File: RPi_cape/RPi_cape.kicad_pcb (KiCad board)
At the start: 4 copper layers, 104 x 255 mm, 523 parts, among them J1 Conn_01x04, J10 Conn_01x02, J11 Conn_01x02, J12 Conn_01x02, J13 Conn_01x02, J14 Conn_01x02, J16 Conn_01x06, J17 Pressure_sensor_barb, J18 Pressure_sensor_barb, J19 Pressure_sensor_barb, J2 Conn_01x02, J20 Pressure_sensor_barb, J3 Conn_01x02, J4 Conn_01x02, J5 Conn_01x03, J6 Conn_01x03, J7 Conn_01x02, J8 Conn_02x20_Odd_Even, J9 Conn_01x02, P15 Conn_02x05_Odd_Even, Q1 MMBT3904, Q10 MMBT3904, Q11 MMBT3904, Q12 MMBT3906, Q13 MMBT3904, Q2 MMBT3904, Q5 MMBT3904, Q6 MMBT3904, Q7 DNP, Q8 MMBT3904, Q9 MMBT3904, U1 TL431A, U10 MS5803-05BA, U11 LM2903, U12 LMC7101B, U13 LMC7101B, U14 BMP388, U15 MS5803-05BA, U16 BMP388, U17 LM2903, U18 74LVC1G08, U19 TPS1H100B, U2 ADC128D818, U20 74LVC1G08, U21 TPS1H100B, U22 74LVC1G08, U23 TPS1H100B, U24 TL431A, U25 LM2903, U26 MIC1557, U27 MIC1557, U28 LM4871M, U29 LP5907MFX-3.3, U3 ADC128D818, U30 LP5907MFX-1.8, U31 DNP (5M40ZE64), U32 MIC1557, U33 5M80ZT100 / 5M240ZT100, U34 LMZ14203, U35 LMZ14203, U36 LMC7101B, U37 LMC7101B, U38 LMC7101B, U4 AD8552A, U5 LM2903, U6 LMC7101B, U7 LMC7101B, U8 74LVC1G08, U9 TPS1H100B

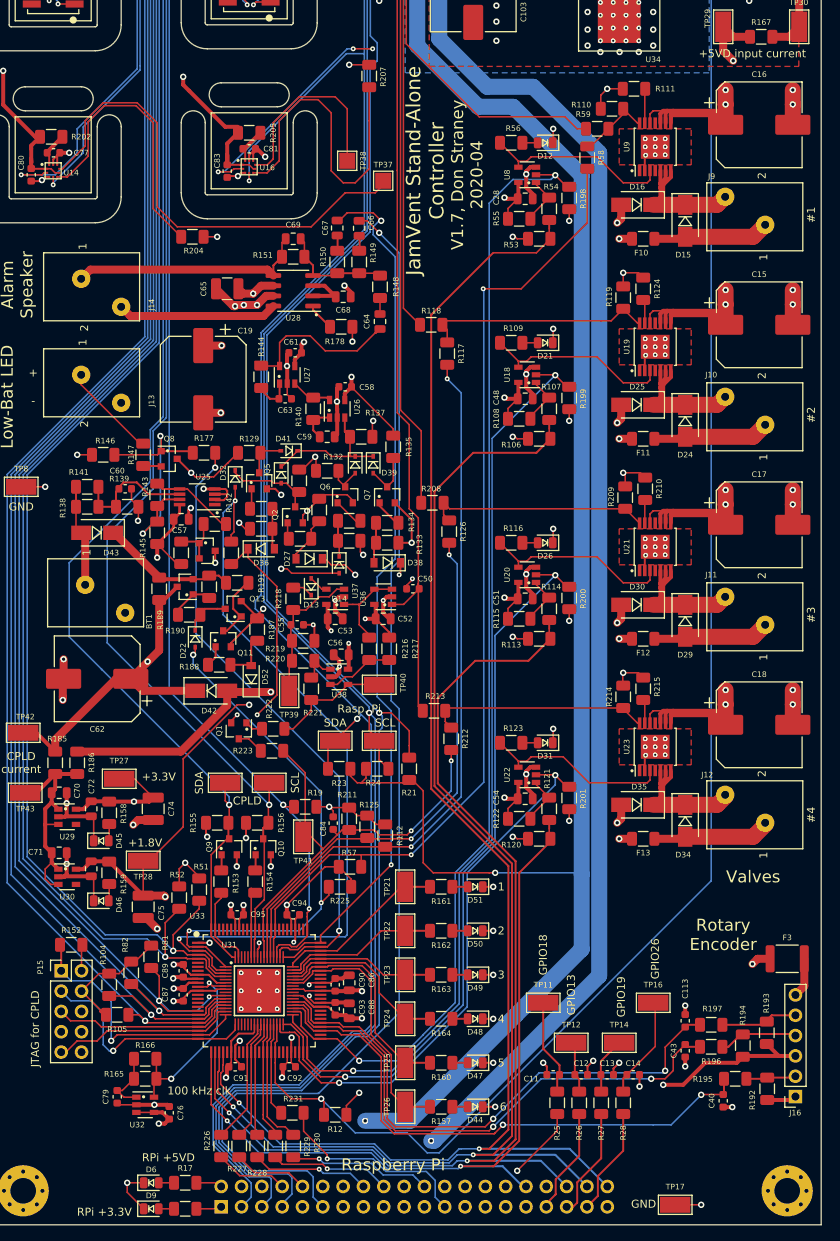
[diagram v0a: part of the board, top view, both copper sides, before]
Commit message: Analog upgrades and extra encoder connectors
Renamed a few files
Removed "costing BOM" as difficult to keep up to date, easy to regenerate
Toughened under-voltage detect circuits by adding hysteresis to +5V detect for +BATT diode-OR (R236), filtering to power-down alarm detect input (C85)
Added connector options (J15, J21) for Grayhill C14-series rotary encoder with cable
Changed R190 from 3K to 2.4K to increase overhead on base current required for saturation, and consolidate BOM
Added 3 solderable testpoints for expanding CPLD pin options (TP44-46), adjusted some CPLD pin assignments to allow physical routing to pins
Fixed valve motion detector by changing comparator's hysteresis to AC-only, changing NPN's series resistor to 1K (allows low-enough DC level to count as logic low), and adding optional filtering cap C115 to offset divider
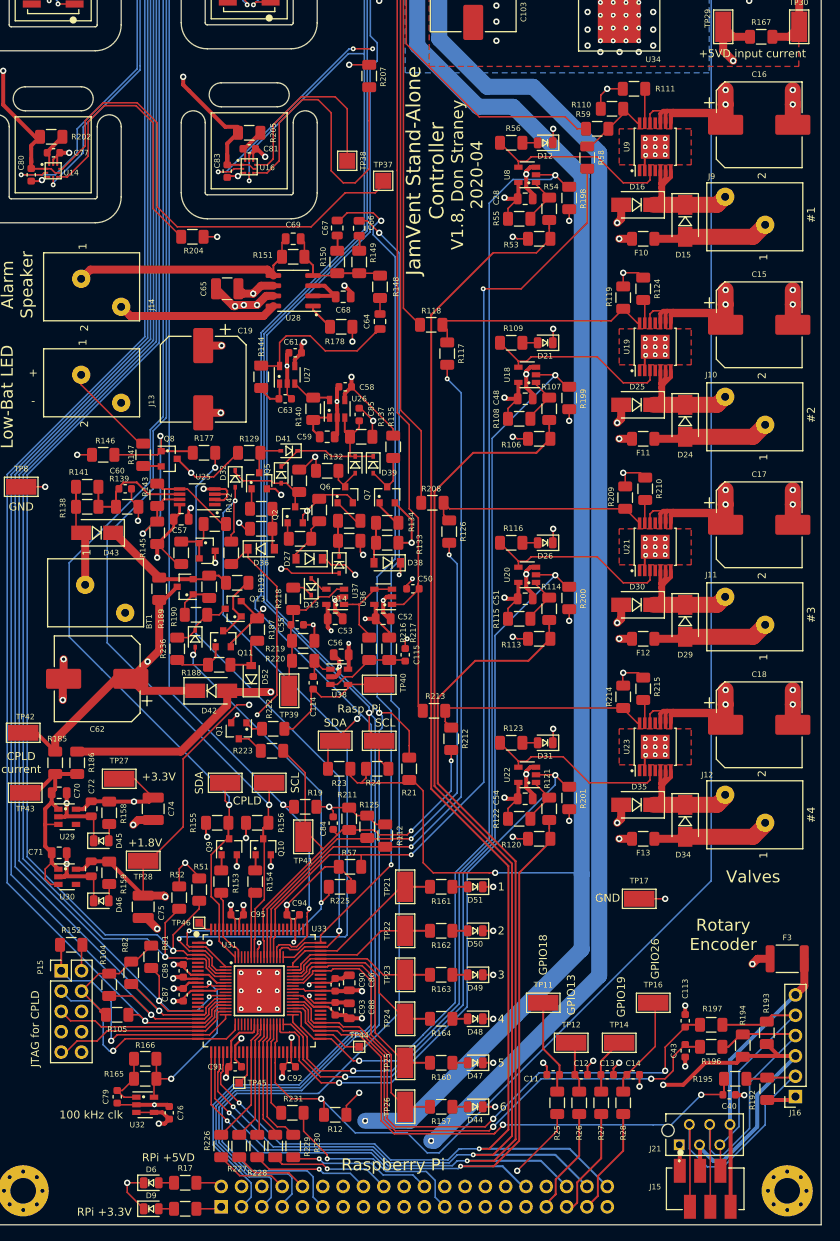
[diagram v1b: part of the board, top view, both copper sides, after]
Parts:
- removed R221: 1M, Resistor_SMD:R_1206_3216Metric
- added C114: 100pF 50V NP0, Capacitor_SMD:C_0603_1608Metric, F.Cu at (69.0, 215.8)
- added C115: DNP, Capacitor_SMD:C_0603_1608Metric, F.Cu at (80.5, 212.2)
- added C85: 100nF 50V X7R, Capacitor_SMD:C_0603_1608Metric, F.Cu at (74.8, 182.2)
- added J15: Conn_01x06, Ventilator:TE_188275-6, F.Cu at (118.0, 279.0)
- added J21: Conn_01x06, Ventilator:TE_215079-6, F.Cu at (114.8, 273.5)
- added R236: 1M, Resistor_SMD:R_1206_3216Metric, F.Cu at (52.0, 211.5)
- added TP44: TestPoint, TestPoint:TestPoint_Pad_1.0x1.0mm, F.Cu at (74.8, 261.2)
- added TP45: TestPoint, TestPoint:TestPoint_Pad_1.0x1.0mm, F.Cu at (59.8, 265.8)
- added TP46: TestPoint, TestPoint:TestPoint_Pad_1.0x1.0mm, F.Cu at (54.8, 245.8)
- R190: value 3K -> 2.4K
- R220: value 1K -> 1M
- R223: value 100K -> 1K
- moved TP17 38.5 mm to (109.8, 242.8)
- moved C40 1.06 mm to (121.0, 267.2), turned to 180 degrees
- moved R190 0.85 mm to (54.4, 207.2)
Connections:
- U33 pad 100: /CPLD_SDA -> Net-(TP46-Pad1)
- U33 pad 35: /CPLD/Comms1 -> Net-(TP45-Pad1)
- U33 pad 36: /CPLD/Comms2 -> /CPLD/Comms1
- U33 pad 37: /CPLD/Comms3 -> /CPLD/Comms2
- U33 pad 38: Net-(U33-Pad38) -> /CPLD/Comms3
- U33 pad 97: Net-(U33-Pad97) -> /CPLD/SDA_Drive
- U33 pad 98: Net-(U33-Pad98) -> /CPLD_SDA
- U33 pad 99: /CPLD/SDA_Drive -> Net-(U33-Pad99)
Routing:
- net Net-(J15-Pad4): track 9.88 -> 43.9 mm
- net Net-(J15-Pad2): track 6.26 -> 40.0 mm
- net Net-(F3-Pad2): track 4.98 -> 34.9 mm
- net +3V3: track 229.6 -> 253.7 mm
- net Net-(J15-Pad5): track 9.96 -> 33.5 mm
- net GND: track 559.1 -> 566.5 mm, vias 275 -> 276
- net Net-(TP44-Pad1): track 0.00 -> 5.45 mm
- net Net-(TP45-Pad1): track 0.00 -> 4.24 mm
- net Net-(Q11-Pad1): track 2.64 -> 6.74 mm
- net Net-(C85-Pad2): track 17.7 -> 20.1 mm
- net Net-(D22-Pad1): track 5.53 -> 7.75 mm
- net Net-(C115-Pad2): track 8.61 -> 10.7 mm
- net Net-(TP46-Pad1): track 0.00 -> 1.84 mm
- net Net-(C114-Pad2): track 15.0 -> 16.7 mm
- net /CPLD/SDA_Drive: track 10.3 -> 9.10 mm
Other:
- board text added: "V1.8, Don Straney 2020-04"
- board text removed: "V1.7, Don Straney 2020-04"

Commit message: Updates based on testing, extra documentation
Added thermal calculations, possible thermal-induced problems to fault-condition list
Renamed error calculations file
Added some bringup tests
Changed 24V LED resistors (R20, R22) to 24.9K to consolidate BOM
Adjusted audio amp volume and filtering according to breadboard experiments
Moved bottom-end mounting holes and encoder connectors to avoid interfering mechanically with Raspberry Pi
Replaced under-sized power-ORing diodes with better Schottky option, added heatsinking with copper planes
Improved LMZ14203 heatsinking by removing thermal reliefs, re-arranging input-current-measurement testpoints to increase top-layer copper area
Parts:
- removed D2: ES2B, Ventilator:D_SMA
- C64, C66, C67: value 1uF 16V X7R -> 100nF 50V X7R; footprint Capacitor_SMD:C_0805_2012Metric -> Capacitor_SMD:C_0603_1608Metric
- C69: value DNP -> 10nF 50V NP0; footprint Capacitor_SMD:C_0805_2012Metric -> Capacitor_SMD:C_0603_1608Metric
- D1: value ES2B -> STPS15H100CB; footprint Ventilator:D_SMA -> Package_TO_SOT_SMD:TO-252-2
- R148: value 10K -> 100K
- R151: value 10K -> 24.9K
- R20, R22: value 22K -> 24.9K
- moved R20 22.3 mm to (115.5, 81.2), turned to 180 degrees
- moved D7 18.9 mm to (119.8, 81.2), turned to 180 degrees
- moved TP29 18.8 mm to (138.8, 137.0), turned to 90 degrees
- moved H1 12.2 mm to (137.2, 271.0)
- moved J15 11.0 mm to (127.0, 272.8)
- moved R194 10.8 mm to (131.7, 255.1)
- moved C113 10.8 mm to (124.5, 252.0)
- moved C40 10.8 mm to (130.0, 261.2)
- moved C43 10.8 mm to (124.5, 255.8)
- moved F3 10.8 mm to (137.2, 244.2)
- moved J16 10.8 mm to (138.3, 261.5)
- moved J21 10.8 mm to (123.8, 267.5)
- moved R192 10.8 mm to (134.8, 260.5)
- moved R195 10.8 mm to (130.8, 259.2)
- moved R196 10.8 mm to (127.8, 255.2)
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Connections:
- F1 pad 2: Net-(D1-Pad1) -> Net-(D1-Pad2)
- J1 pad 1: Net-(D1-Pad2) -> Net-(D1-Pad1)
- J1 pad 3: Net-(D2-Pad2) -> Net-(D1-Pad3)
- R3 pad 1: Net-(D1-Pad2) -> Net-(D1-Pad1)
- R3 pad 2: Net-(D1-Pad1) -> Net-(D1-Pad2)
- R4 pad 1: Net-(D1-Pad1) -> Net-(D1-Pad2)
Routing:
- net Net-(D2-Pad2): track 12.2 -> 0.00 mm
- net Net-(D1-Pad3): track 0.00 -> 11.8 mm
- net +5VD: track 351.7 -> 363.4 mm
- net +24V: track 240.7 -> 231.3 mm
- net Net-(D1-Pad2): track 15.6 -> 23.8 mm, vias 0 -> 30
- net /Enc_B: track 68.9 -> 73.4 mm
- net /Enc_A: track 69.9 -> 74.4 mm
- net GNDPWR: track 63.6 -> 59.2 mm
- net GND: track 566.5 -> 570.5 mm
- net Net-(D1-Pad1): track 17.7 -> 20.7 mm
- net /Enc_Sw: track 69.9 -> 72.4 mm
- net Net-(C96-Pad1): track 49.3 -> 47.0 mm
- net +3V3: track 253.7 -> 251.6 mm
- net +24VA: track 325.2 -> 327.0 mm
- added copper zone on B.Cu, net Net-(D1-Pad2)
- added copper zone on F.Cu, net Net-(D1-Pad2)
- added copper zone on In2.Cu, net Net-(D1-Pad2)
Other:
- outline, holes or cut-outs redrawn
- board text added: "V1.9, Don Straney 2020-05"
- board text removed: "V1.8, Don Straney 2020-04"

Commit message: Admin (naming, license), improvements based on testing
Updated name on schematic, PCB silkscreen
Added 3 mounting holes on inside area of board for better mechanical robustness
Removed extra unused pressure sensor barb packages from library
Fixed Phoenix spring connector footprints, and added 3D models from Phoenix website
Added 3D models to TE encoder connector footprints, QFP-100 for CPLD, and 5019 testpoint
Changed DIAG_EN pin connection from valve drivers from +24V (too high) to +3.3V
Added CERN licensing terms
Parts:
- added H5: #4/M3, MountingHole:MountingHole_3.2mm_M3_Pad_Via, F.Cu at (87.5, 79.5)
- added H6: #4/M3, MountingHole:MountingHole_3.2mm_M3_Pad_Via, F.Cu at (94.0, 154.0)
- added H7: #4/M3, MountingHole:MountingHole_3.2mm_M3_Pad_Via, F.Cu at (97.0, 211.0)
- J17, J18, J19, J20: footprint Ventilator:Pressure_sensor_barb_inner-lip-expanded-slots -> Ventilator:Pressure_sensor_barb
- TP1, TP10, TP11, TP12, TP13, TP14, TP15, TP16, TP17, TP18, TP19, TP2, TP20, TP21, TP22, TP23, TP24, TP25, TP26, TP27, TP28, TP29, TP3, TP30, TP31, TP32, TP33, TP34, TP35, TP36, TP39, TP4, TP40, TP41, TP42, TP43, TP5, TP6, TP7, TP8, TP9: footprint TestPoint:TestPoint_Keystone_5019_Minature -> Ventilator:TestPoint_Keystone_5019_Minature
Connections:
- U19 pad 12: +24V -> +3V3
- U21 pad 12: +24V -> +3V3
- U23 pad 12: +24V -> +3V3
- U9 pad 12: +24V -> +3V3
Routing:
- net +3V3: track 251.6 -> 316.2 mm, vias 24 -> 28
- net +24V: track 231.3 -> 219.4 mm
- net GND: track 570.5 -> 580.5 mm
- net Net-(J14-Pad2): track 20.0 -> 25.8 mm
- net /Output Driver 4/OutH: track 21.5 -> 26.6 mm
- net Net-(C69-Pad2): track 30.0 -> 25.0 mm
- net /Output Driver 3/OutH: track 21.5 -> 26.5 mm
- net /Output Driver 2/OutH: track 21.5 -> 26.5 mm
- net /Output Driver 1/OutH: track 21.5 -> 26.5 mm
- net Net-(D1-Pad3): track 11.8 -> 6.84 mm
- net Net-(D1-Pad1): track 20.7 -> 15.7 mm
- net /Oxygen Sensor Input/In: track 12.8 -> 7.77 mm
- net +24VA: track 327.0 -> 322.0 mm
- net /Output Driver 3/OutL: track 14.6 -> 9.57 mm
- net /Output Driver 2/OutL: track 14.6 -> 9.57 mm
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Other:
- board text added: "3x"
- board text added: "7x D 3.2 mm"
- board text added: "GlobalVent Stand-Alone Controller"
- board text added: "Licensed under CERN-OHL-S v2"
- board text added: "V1.10, Don Straney 2020-05"
- board text removed: "4x"
- board text removed: "4x D 3.2 mm"
- board text removed: "JamVent Stand-Alone Controller"
- board text removed: "V1.9, Don Straney 2020-05"

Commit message: Design update based on changed software/firmware/pneumatics reqs
Swapped Max V CPLD for Max 10 FPGA
Removed +1.8V regulator and monitoring (in power-down alarm) because Max 10 FPGA has internal regulator
Changed FPGA's valve-enable pull-downs from 1K to 10K because Max 10 floats the outputs during power-up/programming (instead of Max V's internal pull-ups)
Changed low-pressure sensor from BMP388 to MS5607 for more manufacturable footprint / high availability, and moved all digital pressure sensors to daughterboard for repairability
Changed single op-amps in analog pressure sensor inputs / valve motion detect circuits to TLV6001 for better bias current, correct footprint
Removed excessive DNP components in analog pressure sensor inputs to ease routing with new op-amps
Added double-inverted hysteresis circuit to valve motion detect that won't drive U38's '+' input above the rail and cause latchup
Added optional pull-down resistors to valve-motiion-detect op-amps to allow output voltages to swing to zero
Added optional filter caps to ADC sensor inputs
Added pull-down to O2 sensor input for testing with sensor unplugged
Increased ADC input resistors (in analog sensor inputs) from 1K to 3.3K to avoid "lifting" +3.3V rail voltage in case of fault
Increased hole sizes to 3.7 mm for fitting #6 screws, to match some threaded vibration-damping bumpers from Joost
Fixed F.Fab-layer component reference text in custom footprints
Updated manufacturing files
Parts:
- removed C78, C80, C82, C83: 100nF 50V X7R, Capacitor_SMD:C_0603_1608Metric
- removed D40: BAS21AH, Ventilator:D_SOD-323
- removed D46: Orange, Ventilator:LED_0805_2012Metric
- removed H5, H6: #4/M3, MountingHole:MountingHole_3.2mm_M3_Pad_Via
- removed J19, J20: Pressure_sensor_barb, Ventilator:Pressure_sensor_barb
- removed Q10, Q6, Q9: MMBT3904, Ventilator:SOT-23
- removed R203, R204, R206, R207, R38, R67, R68: 0, Resistor_SMD:R_1206_3216Metric
- removed R65, R66: DNP, Resistor_SMD:R_1206_3216Metric
- removed TP20, TP28: TestPoint_Flag, Ventilator:TestPoint_Keystone_5019_Minature
- removed TP37, TP38: TestPoint, TestPoint:TestPoint_Pad_2.0x2.0mm
- removed U14, U16: BMP388, Ventilator:Bosch_BMP388
- removed U15: MS5803-05BA, Ventilator:TE_MS5803-05BA
- removed U31: DNP (5M40ZE64), Ventilator:QFP40P900X900X120-65N
- removed U33: 5M80ZT100 / 5M240ZT100, Ventilator:QFP50P1600X1600X120-100N
- added C116: 100nF 50V X7R, Capacitor_SMD:C_0603_1608Metric, F.Cu at (83.5, 245.5)
- added C117: 100nF 50V X7R, Capacitor_SMD:C_0603_1608Metric, F.Cu at (57.8, 245.0)
- added C118: 100nF 50V X7R, Capacitor_SMD:C_0603_1608Metric, F.Cu at (83.5, 241.0)
- added C119: 100nF 50V X7R, Capacitor_SMD:C_0603_1608Metric, F.Cu at (57.8, 259.8)
- added C120: 100nF 50V X7R, Capacitor_SMD:C_0603_1608Metric, F.Cu at (57.8, 242.0)
- added C121: 100nF 50V X7R, Capacitor_SMD:C_0603_1608Metric, F.Cu at (80.5, 239.2)
- added C122: 10pF 50V NP0, Capacitor_SMD:C_0603_1608Metric, F.Cu at (56.0, 250.0)
- added C123: 100nF 50V X7R, Capacitor_SMD:C_0603_1608Metric, F.Cu at (57.8, 261.5)
- added C124: 100nF 50V X7R, Capacitor_SMD:C_0603_1608Metric, F.Cu at (77.0, 238.5)
- added C125: 100nF 50V X7R, Capacitor_SMD:C_0603_1608Metric, F.Cu at (84.2, 243.2)
- added C126: 100nF 50V X7R, Capacitor_SMD:C_0603_1608Metric, F.Cu at (61.0, 264.2)
- added C127: 100nF 50V X7R, Capacitor_SMD:C_0603_1608Metric, F.Cu at (60.8, 239.2)
- added C128: 100nF 50V X7R, Capacitor_SMD:C_0603_1608Metric, F.Cu at (63.0, 238.5)
- added C129: 100nF 50V X7R, Capacitor_SMD:C_0603_1608Metric, F.Cu at (70.2, 264.2)
- added C130: 100nF 50V X7R, Capacitor_SMD:C_0603_1608Metric, F.Cu at (79.5, 265.0)
- added C131: 100nF 50V X7R, Capacitor_SMD:C_0603_1608Metric, F.Cu at (81.8, 264.2)
- added C132: 100nF 50V X7R, Capacitor_SMD:C_0603_1608Metric, F.Cu at (57.8, 243.5)
- added C133: 100nF 50V X7R, Capacitor_SMD:C_0603_1608Metric, F.Cu at (83.5, 261.8)
- added C134: 1uF 16V X7R, Capacitor_SMD:C_0805_2012Metric, F.Cu at (76.8, 266.2)
- added C135: 1uF 16V X7R, Capacitor_SMD:C_0805_2012Metric, F.Cu at (58.8, 237.2)
- added C136: 10pF 50V NP0, Capacitor_SMD:C_0603_1608Metric, F.Cu at (55.4, 251.7)
- added C137: 10pF 50V NP0, Capacitor_SMD:C_0603_1608Metric, F.Cu at (54.5, 256.8)
- added C138: DNP, Capacitor_SMD:C_0603_1608Metric, F.Cu at (62.2, 106.8)
- added C139: DNP, Capacitor_SMD:C_0603_1608Metric, F.Cu at (62.8, 110.8)
- added D2: BAT54C, Package_TO_SOT_SMD:SOT-23, F.Cu at (51.2, 252.8)
- added D33: BAS21AH, Ventilator:D_SOD-323, F.Cu at (73.8, 184.5)
- added FB1: TBD, Inductor_SMD:L_0805_2012Metric, F.Cu at (80.0, 268.2)
- added Q3: MMBT3904, Ventilator:SOT-23, F.Cu at (58.5, 225.8)
- added R221: 0, Resistor_SMD:R_1206_3216Metric, F.Cu at (63.8, 268.9)
- added R237: 10K, Resistor_SMD:R_1206_3216Metric, F.Cu at (62.0, 234.3)
- added R238: 10K, Resistor_SMD:R_1206_3216Metric, F.Cu at (50.4, 262.8)
- added R239: 10K, Resistor_SMD:R_1206_3216Metric, F.Cu at (48.2, 252.3)
- added R240: 100K, Resistor_SMD:R_1206_3216Metric, F.Cu at (83.2, 216.5)
- C114: value 100pF 50V NP0 -> DNP
- C24, C25, C36, C37: footprint Capacitor_SMD:C_0805_2012Metric -> Capacitor_SMD:C_0603_1608Metric
- C71, C73: value 1uF 16V X7R -> 100nF 50V X7R; footprint Capacitor_SMD:C_0805_2012Metric -> Capacitor_SMD:C_0603_1608Metric
- C75: value DNP -> 100nF 50V X7R; footprint Capacitor_SMD:C_1210_3225Metric -> Capacitor_SMD:C_0603_1608Metric
- C77: value 100nF 50V X7R -> 100pF 50V NP0
- C81: value 100nF 50V X7R -> DNP
- C84: value 10nF 50V NP0 -> DNP
- C86: value 1uF 16V X7R -> 10pF 50V NP0; footprint Capacitor_SMD:C_0805_2012Metric -> Capacitor_SMD:C_0603_1608Metric
- D14: value BAS21AH -> BAT54C; footprint Ventilator:D_SOD-323 -> Package_TO_SOT_SMD:SOT-23
- H1, H2, H3, H4, H7: value #4/M3 -> #6; footprint MountingHole:MountingHole_3.2mm_M3_Pad_Via -> MountingHole:MountingHole_3.7mm_Pad_Via
- J17, J18: value Pressure_sensor_barb -> Conn_02x03_Odd_Even; footprint Ventilator:Pressure_sensor_barb -> Connector_PinHeader_2.54mm:PinHeader_2x03_P2.54mm_Vertical_SMD
- R130: value 1K -> 1M
- R152: value 10K -> 1K
- R153: value 10K -> 0
- R154: value 10K -> DNP
- R159: value 100 -> 10K
- R198, R199, R200, R201: value 1K -> 10K
- R202: value 0 -> DNP
- R220: value 1M -> 0
- R223: value 1K -> 0
- R37: value 0 -> 100K
- R39, R40, R69, R70, R92, R93: value 1K -> 3.3K
- U10: value MS5803-05BA -> Pressure_sensor_daughterboard; footprint Ventilator:TE_MS5803-05BA -> Ventilator:Pressure_sensor_daughterboard_1.2
- U12, U13, U36, U37, U38, U6, U7: value LMC7101B -> TLV6001
- U30: value LP5907MFX-1.8 -> 10M08SAE144C8G; footprint Ventilator:SOT-23-5 -> Ventilator:LQFP50P2200X2200X160-145N
- moved R37 149.3 mm to (61.8, 224.8), turned to 90 degrees
- moved R130 144.6 mm to (49.8, 57.1), turned to 90 degrees
- moved R35 128.6 mm to (87.5, 208.5), turned to 0 degrees
- moved R36 116.1 mm to (81.2, 196.0), turned to 0 degrees
- moved R132 82.4 mm to (58.5, 268.9), turned to 90 degrees
- moved R131 78.0 mm to (56.0, 268.9), turned to 90 degrees
- moved C77 73.3 mm to (83.0, 212.5), turned to 270 degrees
- moved D14 66.2 mm to (50.2, 259.5)
- moved C81 65.1 mm to (78.8, 213.5), turned to 270 degrees
- moved R202 61.3 mm to (77.5, 199.6), turned to 270 degrees
- moved R205 57.6 mm to (78.5, 204.0)
- moved C37 36.2 mm to (66.2, 113.0), turned to 90 degrees
- moved C25 35.8 mm to (67.8, 114.0), turned to 90 degrees
- moved J18 33.2 mm to (77.8, 120.5), turned to 180 degrees
- moved U10 33.0 mm to (37.5, 161.0)
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- renumbered BT1 to J22
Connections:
- C24 pad 1: /Pressure Sensor Input 1/Out -> GND
- C24 pad 2: Net-(C24-Pad2) -> /CPLD_ADC0
- C25 pad 1: Net-(C25-Pad1) -> GND
- C25 pad 2: Net-(C25-Pad2) -> /RPi_ADC0
- C36 pad 1: /Pressure Sensor Input 2/Out -> GND
- C36 pad 2: Net-(C36-Pad2) -> /CPLD_ADC1
- C37 pad 1: Net-(C37-Pad1) -> GND
- C37 pad 2: Net-(C37-Pad2) -> /RPi_ADC1
- C71 pad 2: Net-(C70-Pad2) -> +3V3
- C73 pad 2: +1V8 -> +3V3
- C75 pad 1: +1V8 -> GND
- C75 pad 2: GND -> +3V3
- C77 pad 1: GND -> Net-(C115-Pad2)
- C81 pad 1: GND -> Net-(C114-Pad2)
- C86 pad 2: +1V8 -> /CPLD/TDI
- C87 pad 2: +1V8 -> +3V3
- C90 pad 2: +1V8 -> +3V3
- D14 pad 1: Net-(D14-Pad1) -> /CPLD/TDO
- D14 pad 2: +1V8 -> /CPLD/TDI
- Q1 pad 1: Net-(Q1-Pad1) -> Net-(C81-Pad2)
- R130 pad 2: Net-(D14-Pad1) -> /Oxygen Sensor Input/In
- R131 pad 1: Net-(Q6-Pad1) -> +3V3
- R131 pad 2: Net-(D14-Pad1) -> Net-(R131-Pad2)
- R132 pad 1: Net-(D40-Pad2) -> +3V3
- R132 pad 2: +BATT -> /Auditory Alarm/~FPGA_RST
- R153 pad 1: Net-(Q9-Pad1) -> Net-(R153-Pad1)
- R153 pad 2: /CPLD/SDA_Drive -> +3V3
- R154 pad 1: Net-(Q10-Pad1) -> GND
- R154 pad 2: /CPLD/SCL_Drive -> Net-(R153-Pad1)
- R159 pad 1: Net-(D46-Pad2) -> +3V3
- R159 pad 2: +1V8 -> Net-(R159-Pad2)
- R180 pad 2: Net-(C25-Pad1) -> Net-(R180-Pad2)
- R182 pad 2: Net-(C37-Pad1) -> Net-(R182-Pad2)
- R202 pad 1: +3V3 -> Net-(D13-Pad1)
- R202 pad 2: Net-(C77-Pad2) -> Net-(R202-Pad2)
- R205 pad 1: /+3.3V_RPi -> Net-(C55-Pad2)
- R205 pad 2: Net-(C81-Pad2) -> Net-(R202-Pad2)
- R222 pad 1: Net-(Q1-Pad1) -> Net-(C81-Pad2)
- R35 pad 1: GND -> Net-(R216-Pad2)
- R35 pad 2: Net-(C24-Pad2) -> GND
- R36 pad 1: GND -> Net-(D13-Pad2)
- R36 pad 2: Net-(C25-Pad2) -> GND
- R37 pad 1: /Pressure Sensor Input 1/Out -> Net-(D33-Pad2)
- R37 pad 2: Net-(C24-Pad2) -> +3V3
- R39 pad 2: Net-(C25-Pad1) -> Net-(R180-Pad2)
- R69 pad 2: Net-(C37-Pad1) -> Net-(R182-Pad2)
- U10 pad 1: /CPLD_SCL -> GND
- U12 pad 1: Net-(R63-Pad1) -> /Pressure Sensor Input 2/Out
- U12 pad 3: Net-(C36-Pad2) -> Net-(R63-Pad1)
- U13 pad 1: Net-(R64-Pad1) -> Net-(R182-Pad2)
- U13 pad 3: Net-(C37-Pad2) -> Net-(R64-Pad1)
- U13 pad 4: Net-(C37-Pad1) -> Net-(R182-Pad2)
- U30 pad 1: Net-(C70-Pad2) -> +3V3
- U30 pad 2: GND -> /CPLD/+3.3VA
- U30 pad 3: Net-(C70-Pad2) -> GND
- U30 pad 4: Net-(U30-Pad4) -> GND
- U30 pad 5: +1V8 -> +3V3
- U36 pad 1: /CPLD_ADC3 -> Net-(R216-Pad2)
- U36 pad 3: Net-(R216-Pad2) -> /CPLD_ADC3
- U37 pad 1: Net-(R216-Pad2) -> Net-(D13-Pad2)
- U37 pad 3: Net-(C55-Pad2) -> Net-(R216-Pad2)
- U37 pad 4: Net-(D13-Pad2) -> Net-(R202-Pad2)
- U38 pad 1: Net-(C114-Pad1) -> Net-(C114-Pad2)
- U38 pad 3: Net-(C115-Pad2) -> Net-(C114-Pad1)
- U38 pad 4: Net-(C114-Pad2) -> Net-(C115-Pad2)
- U6 pad 1: Net-(R33-Pad1) -> /Pressure Sensor Input 1/Out
- U6 pad 3: Net-(C24-Pad2) -> Net-(R33-Pad1)
- U7 pad 1: Net-(R34-Pad1) -> Net-(R180-Pad2)
- U7 pad 3: Net-(C25-Pad2) -> Net-(R34-Pad1)
- U7 pad 4: Net-(C25-Pad1) -> Net-(R180-Pad2)
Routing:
- net +1V8: track 126.7 -> 0.00 mm, vias 5 -> 0
- net Net-(D33-Pad2): track 0.00 -> 81.9 mm, vias 0 -> 2
- net /CPLD_SCL: track 243.6 -> 163.8 mm, vias 5 -> 2
- net /+3.3V_RPi: track 347.8 -> 275.9 mm, vias 5 -> 4
- net /CPLD_SDA: track 239.9 -> 168.4 mm, vias 5 -> 2
- net Net-(TP37-Pad1): track 61.2 -> 0.00 mm
- net /Auditory Alarm/~FPGA_RST: track 0.00 -> 54.7 mm, vias 0 -> 3
- net Net-(R203-Pad1): track 50.4 -> 0.00 mm
- net /RPi_SDA: track 269.3 -> 219.5 mm, vias 4 -> 3
- net /RPi_SCL: track 276.1 -> 226.7 mm, vias 8 -> 3
- net Net-(R207-Pad1): track 40.5 -> 0.00 mm
- net Net-(R204-Pad1): track 34.8 -> 0.00 mm
- net +3V3: track 316.2 -> 348.5 mm, vias 28 -> 45
- net /CPLD_Alarm_Spkr: track 110.2 -> 79.6 mm
- net Net-(R221-Pad1): track 0.00 -> 30.6 mm, vias 0 -> 2
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- added copper zone on F.Cu, net /CPLD/+3.3VA
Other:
- outline, holes or cut-outs redrawn
- board text added: "+3.3V_RPi"
- board text added: "9x D 3.7 mm"
- board text added: "CPLD_SCL"
- board text added: "CPLD_SDA"
- board text added: "FPGA"
- board text added: "GlobalVent Controller"
- board text added: "NOTES: 1. Assembly to meet IPC-A-610 Class 2 standards 2. Polarity marks: a. Dots and bevels near ICs and modules indicate pin 1 b. '+' symbols near polarized capacitors indicate positive terminal c. Bands near diodes indicate cathode, although standard diode symbols are used wherever possible If polarity issues arise, please e-mail for clarification (understood that this may delay order) 3. No t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"
- board text added: "RPi_SCL"
- board text added: "RPi_SDA"
- board text added: "V1.11, Don Straney 2020-05"
- board text removed: "+1.8V"
- board text removed: "2.50 mm"
- board text removed: "2x"
- board text removed: "2x R 1.00 mm"
- board text removed: "4x Slot 10 x 3 mm"
- board text removed: "4x Slot, 3 mm width"
- board text removed: "6x R 3.25 mm"
- board text removed: "7x D 3.2 mm"
- board text removed: "8x R 0.25 mm"
- board text removed: "CPLD"
- board text removed: "GlobalVent Stand-Alone Controller"
- board text removed: "NOTES: 1. Assembly to meet IPC-A-610 Class 2 standards 2. Modules U14, U16 have special requirements, as listed in the included Bosch BMP388 Handling & Soldering Guidelines. Most important requirements are... a. must not be soldered using a vapor-phase process, b. hole in top of casing must be covered during any liquid or aerosol process (such as cleaning) by a piece of polyimide tape or similar,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"
- board text removed: "V1.10, Don Straney 2020-05"
